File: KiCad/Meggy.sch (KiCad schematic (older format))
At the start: 26 parts, among them J1 USB_B_Micro, J2 Conn_01x03, Q1 DMP2305U-7, Q2 DMP2305U-7, Q3 DMP2305U-7, SW1 SW_Push, SW2 SW_Push, U1 ROM-socket-42pin, U2 AT90USB1286-MU, U3 M29F160F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

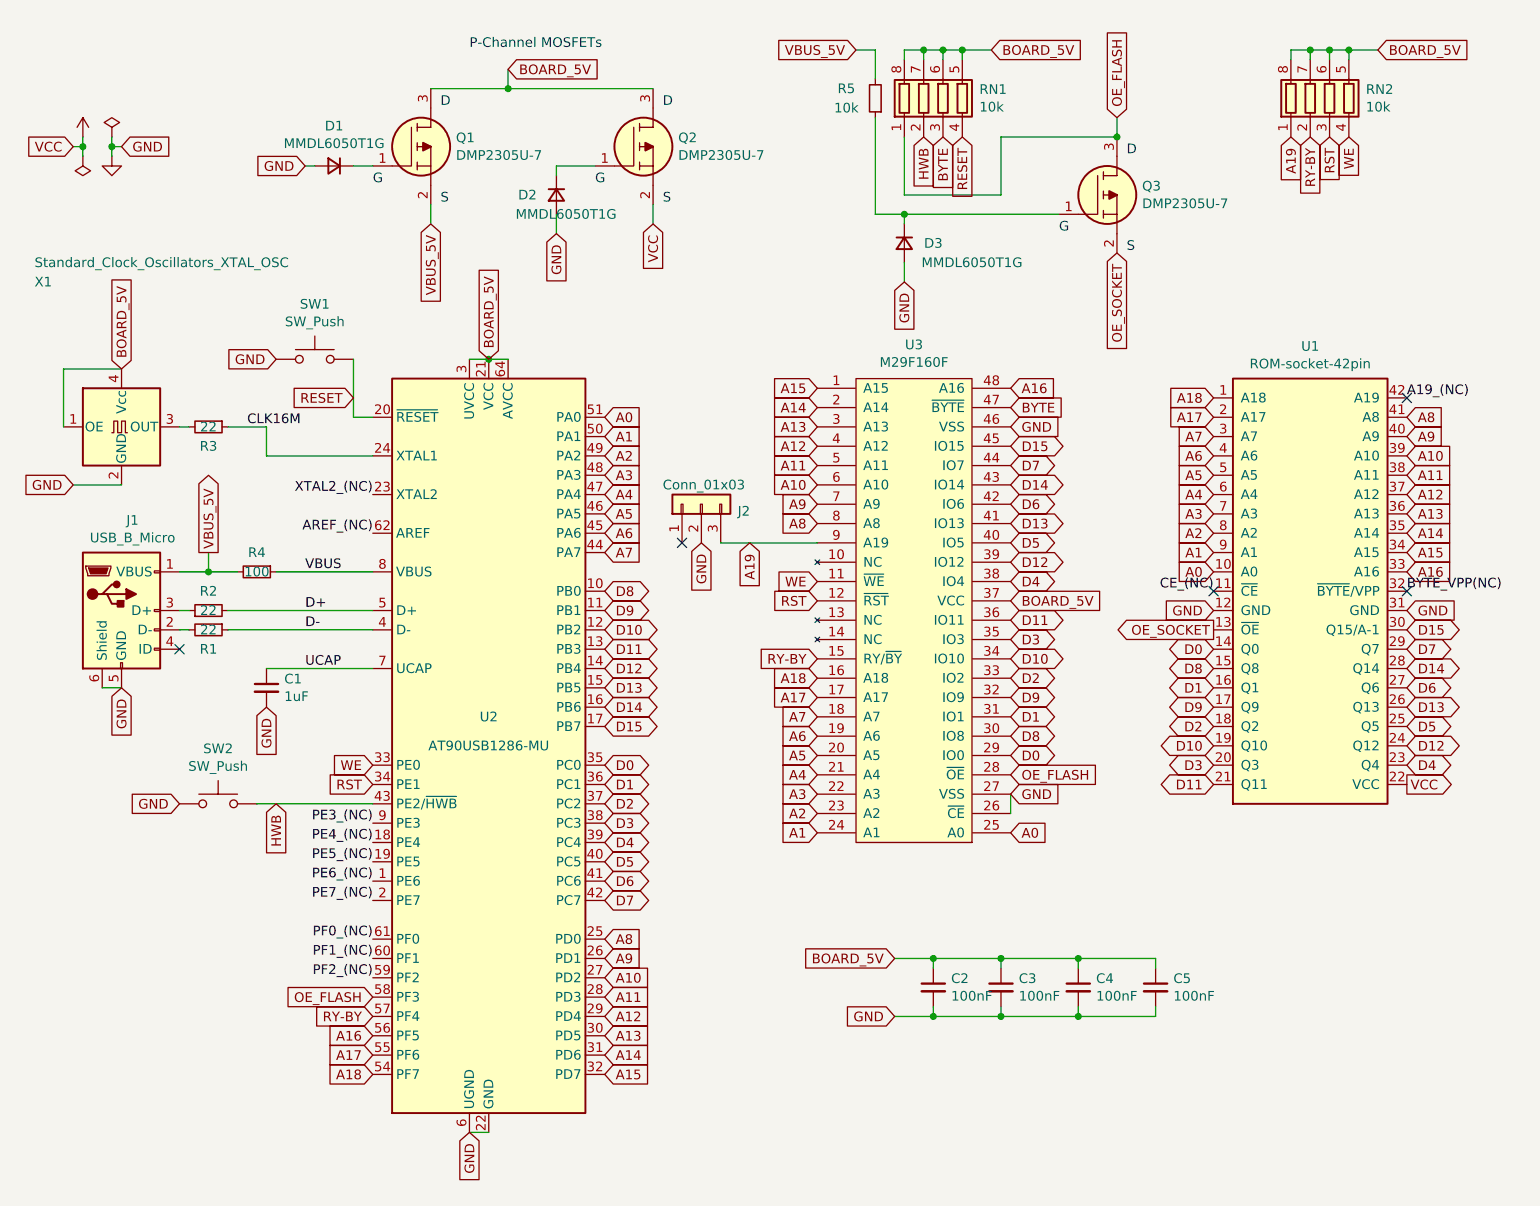
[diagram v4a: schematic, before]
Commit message: Remove Q3 and D3, replace with 74AHCT1G126GW and route OE_SOCKET_EN from pin PE4
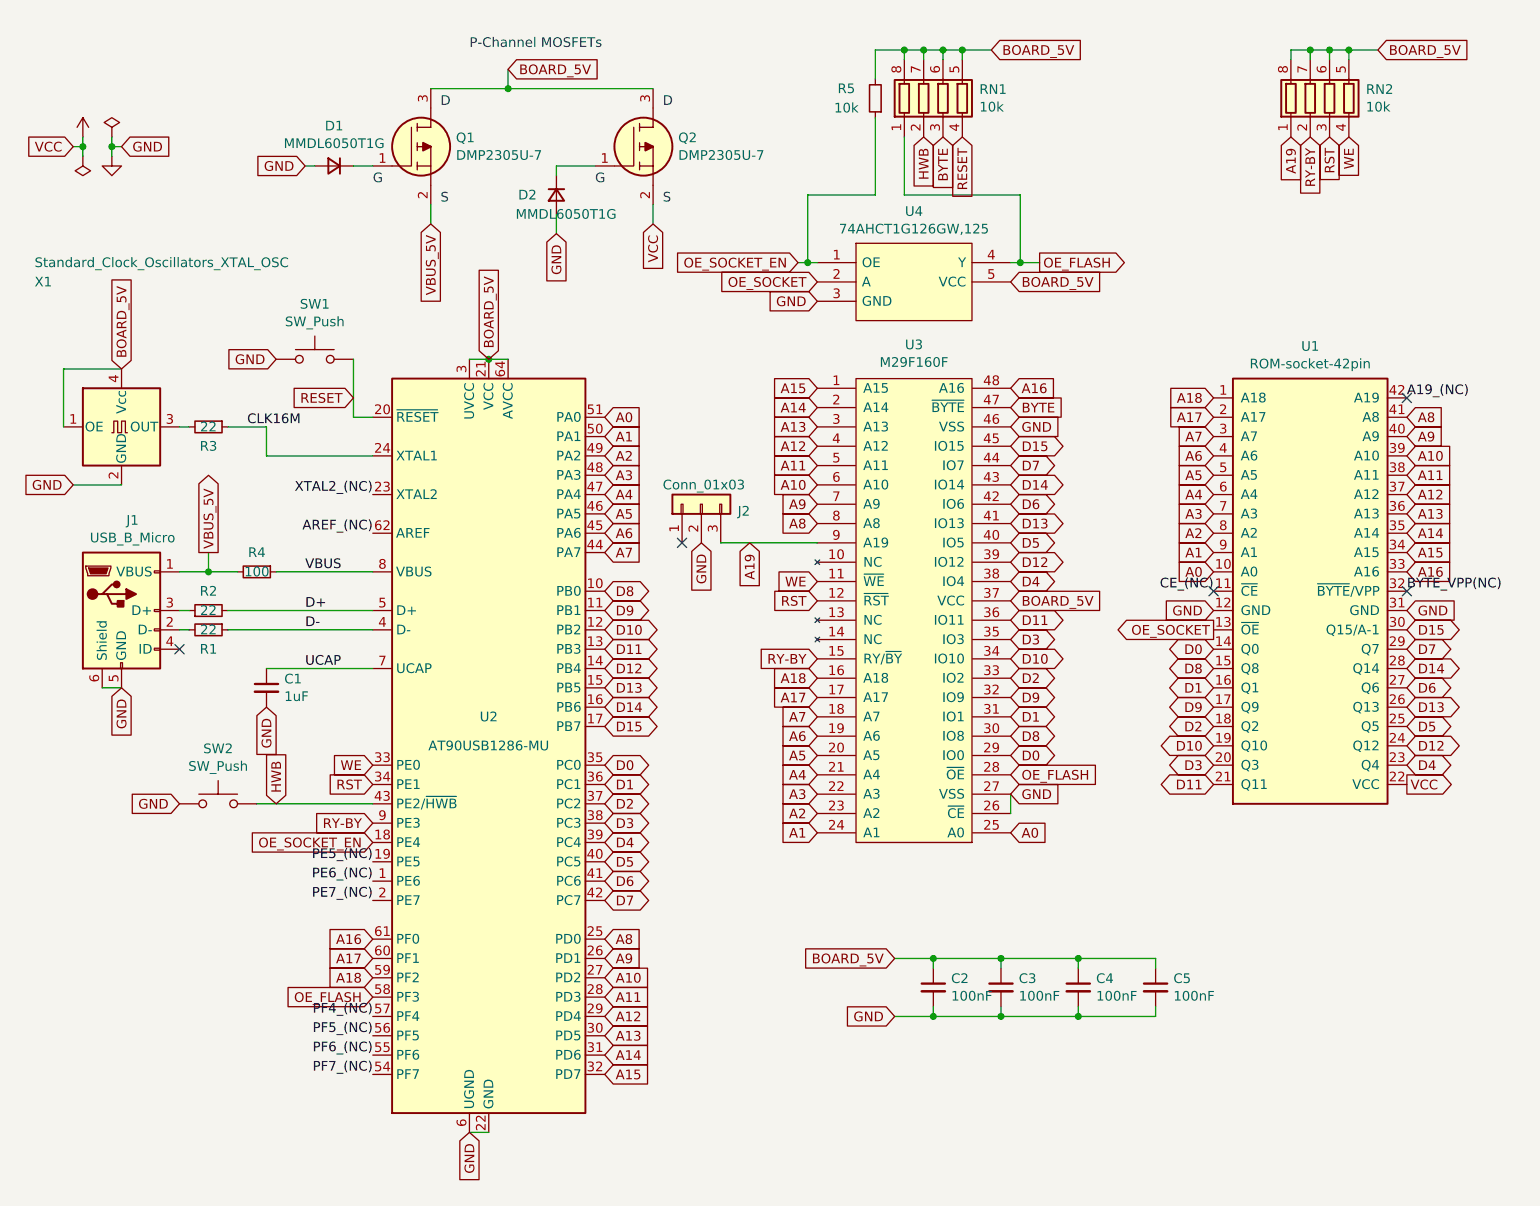
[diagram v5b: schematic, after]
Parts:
- removed D3: MMDL6050T1G, Diode_SMD:D_SOD-523, symbol Device:D_Small
- removed Q3: DMP2305U-7, Package_TO_SOT_SMD:SOT-23, symbol Meggy:DMP2305U-7
- added U4: 74AHCT1G126GW,125, Package_TO_SOT_SMD:SOT-353_SC-70-5, symbol Meggy:74AHCT1G126GW,125
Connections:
- net PE3_(NC) is gone; now on net RY-BY: U2.9 (PE3)
- net PE4_(NC) is gone; now on net OE_SOCKET_EN: U2.18 (PE4)
- net PF0_(NC) is gone; now on net A16: U2.61 (PF0)
- net PF1_(NC) is gone; now on net A17: U2.60 (PF1)
- net PF2_(NC) is gone; now on net A18: U2.59 (PF2)
- net A16: no longer U2.56 (PF5)
- net A17: no longer U2.55 (PF6)
- net A18: no longer U2.54 (PF7)
- net BOARD_5V: now also R5.2, U4.5 (VCC)
- net GND: now also U4.3 (GND)
- net OE_FLASH: now also U4.4 (Y)
- net OE_SOCKET: now also U4.2 (A)
- net RY-BY: no longer U2.57 (PF4)
- net VBUS_5V: no longer R5.2
- net OE_SOCKET_EN: now reaches R5.1
- net OE_SOCKET_EN: now also U4.1 (OE)
- new net PF4_(NC): U2.57 (PF4)
- new net PF5_(NC): U2.56 (PF5)
- new net PF6_(NC): U2.55 (PF6)
- new net PF7_(NC): U2.54 (PF7)
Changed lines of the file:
@@
 Text GLabel 3750 5950 2    50   Input ~ 0
 A15
-Text GLabel 2550 5750 0    50   Input ~ 0
+Text GLabel 2550 5250 0    50   Input ~ 0
 A16
-Text GLabel 2550 5950 0    50   Input ~ 0
+Text GLabel 2550 5450 0    50   Input ~ 0
 A18
 Text GLabel 2450 2450 0    50   Input ~ 0
 RESET
-Text GLabel 2050 4550 3    50   Input ~ 0
+Text GLabel 2050 4550 1    50   Input ~ 0
 HWB
 Text GLabel 4850 3400 0    50   Input ~ 0
@@
 Text GLabel 5850 4400 2    50   Input ~ 0
 OE_FLASH
-Text GLabel 2550 5650 0    50   Input ~ 0
+Text GLabel 2550 4650 0    50   Input ~ 0
 RY-BY
 Text GLabel 3750 2650 2    50   Input ~ 0
@@
 Text GLabel 6900 3250 0    50   Input ~ 0
 A1
-Text GLabel 2550 5850 0    50   Input ~ 0
+Text GLabel 2550 5350 0    50   Input ~ 0
 A17
 $Comp
@@
 Wire Wire Line
 	3500 1500 3500 1600
-$Comp
-L Meggy:DMP2305U-7 Q3
-U 1 1 68E4900A
-P 6100 1500
-F 0 "Q3" H 6530 1646 50  0000 L CNN
-F 1 "DMP2305U-7" H 6530 1555 50  0000 L CNN
-F 2 "Package_TO_SOT_SMD:SOT-23" H 6550 1450 50  0001 L CNN
-F 3 "https://www.diodes.com//assets/Datasheets/DMP2305U.pdf" H 6550 1350 50  0001 L CNN
-	1    6100 1500
-	1    0    0    -1
-$EndComp
-Text GLabel 6400 1000 1    50   Input ~ 0
+Text GLabel 6000 1750 2    50   Output ~ 0
 OE_FLASH
-Text Notes 6100 1600 0    50   ~ 0
-G
-Text Notes 6450 1200 0    50   ~ 0
-D
-Text Notes 6450 1700 0    50   ~ 0
-S
 $Comp
 L Device:R_Pack04 RN1
@@
 	1    0    0    -1
 $EndComp
-Wire Wire Line
-	5300 1500 6100 1500
-$Comp
-L Device:D_Small D3
-U 1 1 68E5A0C5
-P 5300 1650
-F 0 "D3" V 5300 1800 50  0000 C CNN
-F 1 "MMDL6050T1G" V 5400 2000 50  0000 C CNN
-F 2 "Diode_SMD:D_SOD-523" V 5300 1650 50  0001 C CNN
-F 3 "~" V 5300 1650 50  0001 C CNN
-	1    5300 1650
-	0    1    1    0
-$EndComp
-Wire Wire Line
-	5300 1550 5300 1500
-Text GLabel 5300 1850 3    50   Input ~ 0
-GND
-Wire Wire Line
-	5300 1850 5300 1750
+Text GLabel 4850 1950 0    50   Input ~ 0
+GND
 Text GLabel 5750 650  2    50   Input ~ 0
 BOARD_5V
@@
 Wire Wire Line
 	5600 650  5750 650
-Wire Wire Line
-	6400 1000 6400 1100
 Text GLabel 5600 1100 3    50   Input ~ 0
 RESET
-Text GLabel 5050 650  0    50   Input ~ 0
-VBUS_5V
-Wire Wire Line
-	5300 1500 5150 1500
-Connection ~ 5300 1500
 Wire Wire Line
 	5300 1100 5300 1400
-Wire Wire Line
-	5300 1400 5800 1400
-Wire Wire Line
-	5800 1400 5800 1100
-Wire Wire Line
-	5800 1100 6400 1100
-Connection ~ 6400 1100
 Wire Wire Line
 	5400 650  5300 650
@@
 $EndComp
 Wire Wire Line
-	5050 650  5150 650
-Wire Wire Line
 	5150 650  5150 800
-Wire Wire Line
-	5150 1000 5150 1500
 Wire Wire Line
 	1700 3250 1700 3350
@@
 Text GLabel 2550 5550 0    50   Input ~ 0
 OE_FLASH
-Text GLabel 6400 1700 3    50   Input ~ 0
+Text GLabel 4850 1850 0    50   Input ~ 0
 OE_SOCKET
 Text GLabel 6900 3650 0    50   Output ~ 0
@@
 Text Label 2550 3150 2    50   ~ 0
 AREF_(NC)
-Text Label 2550 4650 2    50   ~ 0
-PE3_(NC)
-Text Label 2550 4750 2    50   ~ 0
-PE4_(NC)
 Text Label 2550 4850 2    50   ~ 0
 PE5_(NC)
@@
 Text Label 2550 5050 2    50   ~ 0
 PE7_(NC)
-Text Label 2550 5250 2    50   ~ 0
-PF0_(NC)
-Text Label 2550 5350 2    50   ~ 0
-PF1_(NC)
-Text Label 2550 5450 2    50   ~ 0
-PF2_(NC)
+Text Label 2550 5750 2    50   ~ 0
+PF5_(NC)
+Text Label 2550 5850 2    50   ~ 0
+PF6_(NC)
+Text Label 2550 5950 2    50   ~ 0
+PF7_(NC)
 Text Label 2550 2950 2    50   ~ 0
 XTAL2_(NC)
+Text Label 2550 5650 2    50   ~ 0
+PF4_(NC)
+$Comp
+L Meggy:74AHCT1G126GW,125 U4
+U 1 1 6A4C29B3
+P 5350 1850
+F 0 "U4" H 5350 2215 50  0000 C CNN
+F 1 "74AHCT1G126GW,125" H 5350 2124 50  0000 C CNN
+F 2 "Package_TO_SOT_SMD:SOT-353_SC-70-5" H 5050 2150 50  0001 L CNN
+F 3 "https://assets.nexperia.com/documents/data-sheet/74AHC_AHCT1G126.pdf" H 5700 1950 50  0001 L CNN
+	1    5350 1850
+	1    0    0    -1
+$EndComp
+Wire Wire Line
+	5150 1400 5150 1000
+Text GLabel 2550 4750 0    50   Input ~ 0
+OE_SOCKET_EN
+Wire Wire Line
+	5850 1750 5900 1750
+Wire Wire Line
+	5900 1750 5900 1400
+Wire Wire Line
+	5300 1400 5900 1400
+Connection ~ 5900 1750
+Wire Wire Line
+	5900 1750 6000 1750
+Text GLabel 4750 1750 0    50   Input ~ 0
+OE_SOCKET_EN
+Wire Wire Line
+	4800 1750 4800 1400
+Wire Wire Line
+	4800 1400 5150 1400
+Wire Wire Line
+	4850 1750 4800 1750
+Wire Wire Line
+	4800 1750 4750 1750
+Connection ~ 4800 1750
+Text GLabel 5850 1850 2    50   Input ~ 0
+BOARD_5V
+Wire Wire Line
+	5150 650  5300 650
+Connection ~ 5300 650
 $EndSCHEMATC

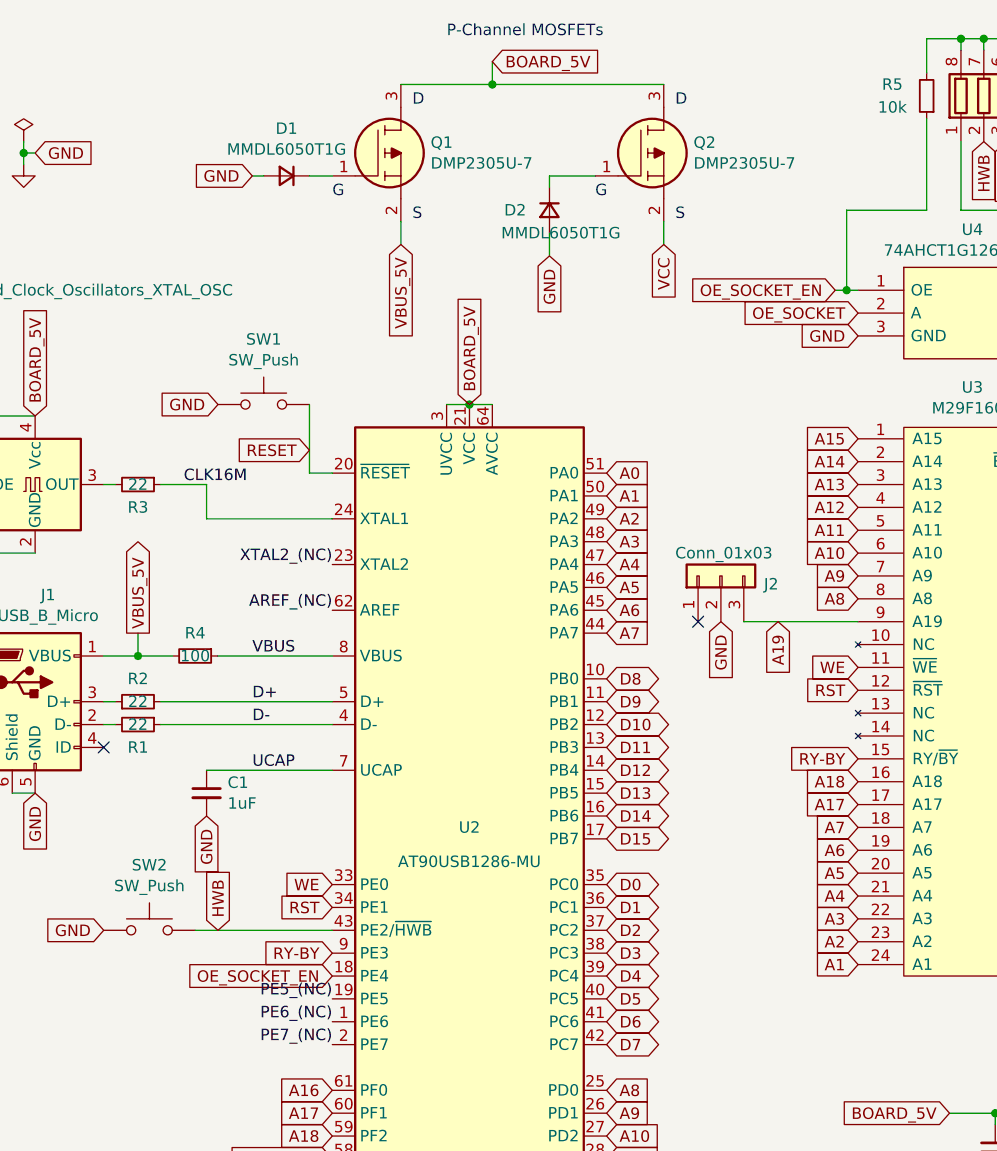
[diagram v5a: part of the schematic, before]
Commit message: Fix pin assignments JTAG conflict, power OR circuit, OE isolation
- Replace P-channel MOSFET power OR (Q1/Q2) with Schottky diodes
- Replace Q3 MOSFET OE isolation with 74AHCT1G126GW tristate buffer (PE4 enable, 10k pull-up)
- Move A16/A17/A18 from PF5/PF6/PF7 (JTAG conflict) to PF0/PF1/PF2
- Move RY/BY from PF4 (JTAG conflict) to PE3
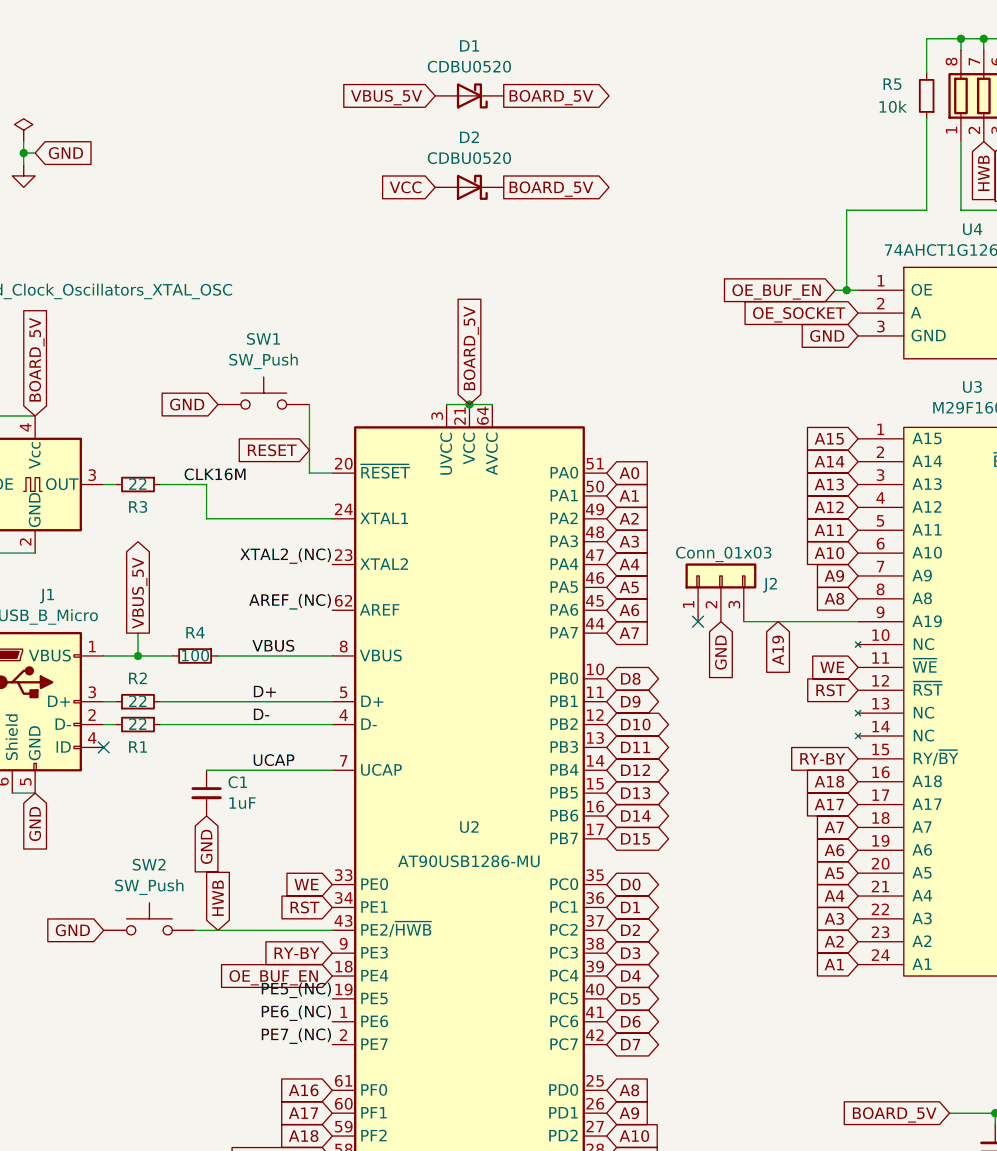
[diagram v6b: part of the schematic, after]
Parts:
- removed D1, D2: MMDL6050T1G, Meggy:D_0603_1608Metric_Pad_0.975x0.95mm_HandSolder, symbol Device:D_Small
- removed Q1, Q2: DMP2305U-7, Package_TO_SOT_SMD:SOT-23, symbol Meggy:DMP2305U-7
- added D1, D2: CDBU0520, Meggy:D_0603_1608Metric_Pad_0.975x0.95mm_HandSolder, symbol Device:D_Schottky
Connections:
- net BOARD_5V: now also D1.1 (K), D2.1 (K)
- net VBUS_5V: now also D1.2 (A)
- net VCC: now also D2.2 (A)
- net OE_SOCKET_EN renamed OE_BUF_EN
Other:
- note removed: "D"
- note removed: "G"
- note removed: "P-Channel MOSFETs"
- note removed: "S"
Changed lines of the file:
@@
 	6600 5650 6600 5600
 Connection ~ 6200 5650
-Text Notes 2550 1350 0    50   ~ 0
-G
-Text Notes 2900 950  0    50   ~ 0
-D
-Text Notes 2900 1450 0    50   ~ 0
-S
-Text Notes 3050 650  0    50   ~ 0
-P-Channel MOSFETs
-Text GLabel 3250 750  2    50   Input ~ 0
-BOARD_5V
-$Comp
-L Meggy:DMP2305U-7 Q1
-U 1 1 68D8212F
-P 2550 1250
-F 0 "Q1" H 2980 1396 50  0000 L CNN
-F 1 "DMP2305U-7" H 2980 1305 50  0000 L CNN
-F 2 "Package_TO_SOT_SMD:SOT-23" H 3000 1200 50  0001 L CNN
-F 3 "https://www.diodes.com//assets/Datasheets/DMP2305U.pdf" H 3000 1100 50  0001 L CNN
-	1    2550 1250
-	1    0    0    -1
-$EndComp
-Text Notes 3700 1350 0    50   ~ 0
-G
-Text Notes 4050 950  0    50   ~ 0
-D
-Text Notes 4050 1450 0    50   ~ 0
-S
-$Comp
-L Meggy:DMP2305U-7 Q2
-U 1 1 68D926EB
-P 3700 1250
-F 0 "Q2" H 4130 1396 50  0000 L CNN
-F 1 "DMP2305U-7" H 4130 1305 50  0000 L CNN
-F 2 "Package_TO_SOT_SMD:SOT-23" H 4150 1200 50  0001 L CNN
-F 3 "https://www.diodes.com//assets/Datasheets/DMP2305U.pdf" H 4150 1100 50  0001 L CNN
-	1    3700 1250
-	1    0    0    -1
-$EndComp
 Text GLabel 1700 3250 1    50   Output ~ 0
 VBUS_5V
-Text GLabel 2850 1550 3    50   Input ~ 0
+Text GLabel 3000 900  0    50   Input ~ 0
 VBUS_5V
-Text GLabel 4000 1550 3    50   Input ~ 0
-VCC
-Wire Wire Line
-	3250 750  3250 850
-Wire Wire Line
-	2850 850  3250 850
-Connection ~ 3250 850
 Text GLabel 2550 4450 0    50   Input ~ 0
 RST
 Text GLabel 2550 4350 0    50   Input ~ 0
 WE
-Wire Wire Line
-	2850 1450 2850 1550
-Wire Wire Line
-	4000 1450 4000 1550
-Text GLabel 2200 1250 0    50   Input ~ 0
-GND
-Wire Wire Line
-	2250 1250 2200 1250
-Text GLabel 3500 1600 3    50   Input ~ 0
-GND
-Wire Wire Line
-	3500 1250 3500 1300
-Wire Wire Line
-	3250 850  4000 850
-$Comp
-L Device:D_Small D1
-U 1 1 68E1A907
-P 2350 1250
-F 0 "D1" H 2350 1043 50  0000 C CNN
-F 1 "MMDL6050T1G" H 2350 1134 50  0000 C CNN
-F 2 "Meggy:D_0603_1608Metric_Pad_0.975x0.95mm_HandSolder" V 2350 1250 50  0001 C CNN
-F 3 "~" V 2350 1250 50  0001 C CNN
-	1    2350 1250
-	-1   0    0    1
-$EndComp
-Wire Wire Line
-	2450 1250 2550 1250
-Wire Wire Line
-	3500 1250 3700 1250
-$Comp
-L Device:D_Small D2
-U 1 1 68E38814
-P 3500 1400
-F 0 "D2" V 3500 1250 50  0000 C CNN
-F 1 "MMDL6050T1G" V 3600 1450 50  0000 C CNN
-F 2 "Meggy:D_0603_1608Metric_Pad_0.975x0.95mm_HandSolder" V 3500 1400 50  0001 C CNN
-F 3 "~" V 3500 1400 50  0001 C CNN
-	1    3500 1400
-	0    1    1    0
-$EndComp
-Wire Wire Line
-	3500 1500 3500 1600
 Text GLabel 6000 1750 2    50   Output ~ 0
 OE_FLASH
@@
 	5150 1400 5150 1000
 Text GLabel 2550 4750 0    50   Input ~ 0
-OE_SOCKET_EN
+OE_BUF_EN
 Wire Wire Line
 	5850 1750 5900 1750
@@
 	5900 1750 6000 1750
 Text GLabel 4750 1750 0    50   Input ~ 0
-OE_SOCKET_EN
+OE_BUF_EN
 Wire Wire Line
 	4800 1750 4800 1400
@@
 	5150 650  5300 650
 Connection ~ 5300 650
+$Comp
+L Device:D_Schottky D1
+U 1 1 6A56256F
+P 3150 900
+F 0 "D1" H 3150 683 50  0000 C CNN
+F 1 "CDBU0520" H 3150 774 50  0000 C CNN
+F 2 "Meggy:D_0603_1608Metric_Pad_0.975x0.95mm_HandSolder" H 3150 900 50  0001 C CNN
+F 3 "~" H 3150 900 50  0001 C CNN
+	1    3150 900
+	-1   0    0    1
+$EndComp
+Text GLabel 3300 900  2    50   Output ~ 0
+BOARD_5V
+$Comp
+L Device:D_Schottky D2
+U 1 1 6A57DF54
+P 3150 1300
+F 0 "D2" H 3150 1083 50  0000 C CNN
+F 1 "CDBU0520" H 3150 1174 50  0000 C CNN
+F 2 "Meggy:D_0603_1608Metric_Pad_0.975x0.95mm_HandSolder" H 3150 1300 50  0001 C CNN
+F 3 "~" H 3150 1300 50  0001 C CNN
+	1    3150 1300
+	-1   0    0    1
+$EndComp
+Text GLabel 3000 1300 0    50   Input ~ 0
+VCC
+Text GLabel 3300 1300 2    50   Output ~ 0
+BOARD_5V
 $EndSCHEMATC
